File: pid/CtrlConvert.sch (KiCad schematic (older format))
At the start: 19 parts

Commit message: [pid] -
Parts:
- added C19, C20: 0.01u, ~, symbol C
- gave numbers to parts that had none: 18
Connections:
- wire segments 47 -> 51

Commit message: [pid] -
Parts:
- renumbered C18 to C17, C17 to C18, C20 to C19, C19 to C20, R37 to R40, R38 to R41, R41 to R42, R42 to R43, R39 to R44, R40 to R45, R44 to R46, R43 to R47, R46 to R48, R45 to R49, RV11 to RV10, RV10 to RV11, RV13 to RV12, RV12 to RV13
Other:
- moved on the sheet: C17, C18, C19, C20, R42, R43, R44, R45, R46, R47, R48, R49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

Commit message: [pid] net list
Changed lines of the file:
@@
 AR Path="/5355C3A0/53598F30/53556034" Ref="U17"  Part="1"
 AR Path="/5362BBC7/53598F30/53556034" Ref="U28"  Part="1"
-F 0 "U4" H 5200 2600 60  0000 C CNN
+F 0 "U28" H 5200 2600 60  0000 C CNN
 F 1 "MAX44251" H 5350 2250 60  0000 C CNN
 F 2 "~" H 4900 2400 60  0000 C CNN
@@
 AR Path="/5355C3A0/53598F30/53556043" Ref="U17"  Part="2"
 AR Path="/5362BBC7/53598F30/53556043" Ref="U28"  Part="2"
-F 0 "U4" H 5200 5450 60  0000 C CNN
+F 0 "U28" H 5200 5450 60  0000 C CNN
 F 1 "MAX44251" H 5350 5100 60  0000 C CNN
 F 2 "~" H 4900 5250 60  0000 C CNN
@@
 AR Path="/5355C3A0/53598F30/53556C67" Ref="R128"  Part="1"
 AR Path="/5362BBC7/53598F30/53556C67" Ref="R179"  Part="1"
-F 0 "R40" V 2680 2350 40  0000 C CNN
+F 0 "R179" V 2680 2350 40  0000 C CNN
 F 1 "100k" V 2607 2351 40  0000 C CNN
 F 2 "~" V 2530 2350 30  0000 C CNN
@@
 $EndComp
 $Comp
-L GND #PWR026
+L GND #PWR030
 U 1 1 53556C85
 P 2600 3300
-AR Path="/5355B409/53598F2F/53556C85" Ref="#PWR026"  Part="1"
-AR Path="/53562461/53555E75/53556C85" Ref="#PWR055"  Part="1"
-AR Path="/5355C3A0/53598F30/53556C85" Ref="#PWR082"  Part="1"
-AR Path="/5362BBC7/53598F30/53556C85" Ref="#PWR0120"  Part="1"
-F 0 "#PWR0120" H 2600 3300 30  0001 C CNN
+AR Path="/5355B409/53598F2F/53556C85" Ref="#PWR030"  Part="1"
+AR Path="/53562461/53555E75/53556C85" Ref="#PWR059"  Part="1"
+AR Path="/5355C3A0/53598F30/53556C85" Ref="#PWR086"  Part="1"
+AR Path="/5362BBC7/53598F30/53556C85" Ref="#PWR0124"  Part="1"
+F 0 "#PWR0124" H 2600 3300 30  0001 C CNN
 F 1 "GND" H 2600 3230 30  0001 C CNN
 F 2 "" H 2600 3300 60  0000 C CNN
@@
 AR Path="/5355C3A0/53598F30/53556CAF" Ref="R129"  Part="1"
 AR Path="/5362BBC7/53598F30/53556CAF" Ref="R180"  Part="1"
-F 0 "R41" V 2680 2950 40  0000 C CNN
+F 0 "R180" V 2680 2950 40  0000 C CNN
 F 1 "2k" V 2607 2951 40  0000 C CNN
 F 2 "~" V 2530 2950 30  0000 C CNN
@@
 AR Path="/5355C3A0/53598F30/53556D28" Ref="C67"  Part="1"
 AR Path="/5362BBC7/53598F30/53556D28" Ref="C102"  Part="1"
-F 0 "C16" H 2400 3050 40  0000 L CNN
+F 0 "C102" H 2400 3050 40  0000 L CNN
 F 1 "10u" H 2406 2865 40  0000 L CNN
 F 2 "~" H 2438 2800 30  0000 C CNN
@@
 AR Path="/5355C3A0/53598F30/53556F13" Ref="RV40"  Part="1"
 AR Path="/5362BBC7/53598F30/53556F13" Ref="RV54"  Part="1"
-F 0 "RV13" H 5050 4550 50  0000 C CNN
+F 0 "RV54" H 5050 4550 50  0000 C CNN
 F 1 "200k" H 5050 4650 50  0000 C CNN
 F 2 "~" H 5050 4650 60  0000 C CNN
@@
 AR Path="/5355C3A0/53598F30/53556F19" Ref="RV38"  Part="1"
 AR Path="/5362BBC7/53598F30/53556F19" Ref="RV52"  Part="1"
-F 0 "RV11" H 3850 4550 50  0000 C CNN
+F 0 "RV52" H 3850 4550 50  0000 C CNN
 F 1 "20k" H 3850 4650 50  0000 C CNN
 F 2 "~" H 3850 4650 60  0000 C CNN
@@
 AR Path="/5355C3A0/53598F30/53556FB4" Ref="R137"  Part="1"
 AR Path="/5362BBC7/53598F30/53556FB4" Ref="R188"  Part="1"
-F 0 "R49" V 5480 4950 40  0000 C CNN
+F 0 "R188" V 5480 4950 40  0000 C CNN
 F 1 "20k" V 5407 4951 40  0000 C CNN
 F 2 "~" V 5330 4950 30  0000 C CNN
@@
 AR Path="/5355C3A0/53598F30/5355702B" Ref="R135"  Part="1"
 AR Path="/5362BBC7/53598F30/5355702B" Ref="R186"  Part="1"
-F 0 "R47" V 4430 4650 40  0000 C CNN
+F 0 "R186" V 4430 4650 40  0000 C CNN
 F 1 "20k" V 4357 4651 40  0000 C CNN
 F 2 "~" V 4280 4650 30  0000 C CNN
@@
 AR Path="/5355C3A0/53598F30/53557349" Ref="R132"  Part="1"
 AR Path="/5362BBC7/53598F30/53557349" Ref="R183"  Part="1"
-F 0 "R44" V 3930 4050 40  0000 C CNN
+F 0 "R183" V 3930 4050 40  0000 C CNN
 F 1 "2k" V 3857 4051 40  0000 C CNN
 F 2 "~" V 3780 4050 30  0000 C CNN
@@
 AR Path="/5355C3A0/53598F30/5355734F" Ref="R133"  Part="1"
 AR Path="/5362BBC7/53598F30/5355734F" Ref="R184"  Part="1"
-F 0 "R45" V 3930 5250 40  0000 C CNN
+F 0 "R184" V 3930 5250 40  0000 C CNN
 F 1 "2k" V 3857 5251 40  0000 C CNN
 F 2 "~" V 3780 5250 30  0000 C CNN
@@
 AR Path="/5355C3A0/53598F30/53557785" Ref="RV37"  Part="1"
 AR Path="/5362BBC7/53598F30/53557785" Ref="RV51"  Part="1"
-F 0 "RV10" H 3850 2400 50  0000 C CNN
+F 0 "RV51" H 3850 2400 50  0000 C CNN
 F 1 "20k" H 3850 2500 50  0000 C CNN
 F 2 "~" H 3850 2500 60  0000 C CNN
@@
 AR Path="/5355C3A0/53598F30/5355778B" Ref="R130"  Part="1"
 AR Path="/5362BBC7/53598F30/5355778B" Ref="R181"  Part="1"
-F 0 "R42" V 3930 1900 40  0000 C CNN
+F 0 "R181" V 3930 1900 40  0000 C CNN
 F 1 "2k" V 3857 1901 40  0000 C CNN
 F 2 "~" V 3780 1900 30  0000 C CNN
@@
 AR Path="/5355C3A0/53598F30/53557791" Ref="R131"  Part="1"
 AR Path="/5362BBC7/53598F30/53557791" Ref="R182"  Part="1"
-F 0 "R43" V 3930 3100 40  0000 C CNN
+F 0 "R182" V 3930 3100 40  0000 C CNN
 F 1 "2k" V 3857 3101 40  0000 C CNN
 F 2 "~" V 3780 3100 30  0000 C CNN
@@
 AR Path="/5355C3A0/53598F30/5355779F" Ref="R134"  Part="1"
 AR Path="/5362BBC7/53598F30/5355779F" Ref="R185"  Part="1"
-F 0 "R46" V 4430 2300 40  0000 C CNN
+F 0 "R185" V 4430 2300 40  0000 C CNN
 F 1 "20k" V 4357 2301 40  0000 C CNN
 F 2 "~" V 4280 2300 30  0000 C CNN
@@
 AR Path="/5355C3A0/53598F30/535579B2" Ref="RV39"  Part="1"
 AR Path="/5362BBC7/53598F30/535579B2" Ref="RV53"  Part="1"
-F 0 "RV12" H 5050 1700 50  0000 C CNN
+F 0 "RV53" H 5050 1700 50  0000 C CNN
 F 1 "200k" H 5050 1800 50  0000 C CNN
 F 2 "~" H 5050 1800 60  0000 C CNN
@@
 AR Path="/5355C3A0/53598F30/535579B8" Ref="R136"  Part="1"
 AR Path="/5362BBC7/53598F30/535579B8" Ref="R187"  Part="1"
-F 0 "R48" V 5480 2100 40  0000 C CNN
+F 0 "R187" V 5480 2100 40  0000 C CNN
 F 1 "20k" V 5407 2101 40  0000 C CNN
 F 2 "~" V 5330 2100 30  0000 C CNN
@@
 AR Path="/5355C3A0/53598F30/53557D04" Ref="C69"  Part="1"
 AR Path="/5362BBC7/53598F30/53557D04" Ref="C104"  Part="1"
-F 0 "C18" H 4050 5000 40  0000 L CNN
+F 0 "C104" H 4050 5000 40  0000 L CNN
 F 1 "10u" H 4056 4815 40  0000 L CNN
 F 2 "~" H 4088 4750 30  0000 C CNN
@@
 AR Path="/5355C3A0/53598F30/53557D0A" Ref="C68"  Part="1"
 AR Path="/5362BBC7/53598F30/53557D0A" Ref="C103"  Part="1"
-F 0 "C17" H 4050 2850 40  0000 L CNN
+F 0 "C103" H 4050 2850 40  0000 L CNN
 F 1 "10u" H 4056 2665 40  0000 L CNN
 F 2 "~" H 4088 2600 30  0000 C CNN
@@
 $EndComp
 $Comp
-L GND #PWR027
+L GND #PWR031
 U 1 1 53557D10
 P 4050 5200
-AR Path="/5355B409/53598F2F/53557D10" Ref="#PWR027"  Part="1"
-AR Path="/53562461/53555E75/53557D10" Ref="#PWR056"  Part="1"
-AR Path="/5355C3A0/53598F30/53557D10" Ref="#PWR083"  Part="1"
-AR Path="/5362BBC7/53598F30/53557D10" Ref="#PWR0121"  Part="1"
-F 0 "#PWR0121" H 4050 5200 30  0001 C CNN
+AR Path="/5355B409/53598F2F/53557D10" Ref="#PWR031"  Part="1"
+AR Path="/53562461/53555E75/53557D10" Ref="#PWR060"  Part="1"
+AR Path="/5355C3A0/53598F30/53557D10" Ref="#PWR087"  Part="1"
+AR Path="/5362BBC7/53598F30/53557D10" Ref="#PWR0125"  Part="1"
+F 0 "#PWR0125" H 4050 5200 30  0001 C CNN
 F 1 "GND" H 4050 5130 30  0001 C CNN
 F 2 "" H 4050 5200 60  0000 C CNN
@@
 $EndComp
 $Comp
-L GND #PWR028
+L GND #PWR032
 U 1 1 53557D16
 P 4050 3050
-AR Path="/5355B409/53598F2F/53557D16" Ref="#PWR028"  Part="1"
-AR Path="/53562461/53555E75/53557D16" Ref="#PWR057"  Part="1"
-AR Path="/5355C3A0/53598F30/53557D16" Ref="#PWR084"  Part="1"
-AR Path="/5362BBC7/53598F30/53557D16" Ref="#PWR0122"  Part="1"
-F 0 "#PWR0122" H 4050 3050 30  0001 C CNN
+AR Path="/5355B409/53598F2F/53557D16" Ref="#PWR032"  Part="1"
+AR Path="/53562461/53555E75/53557D16" Ref="#PWR061"  Part="1"
+AR Path="/5355C3A0/53598F30/53557D16" Ref="#PWR088"  Part="1"
+AR Path="/5362BBC7/53598F30/53557D16" Ref="#PWR0126"  Part="1"
+F 0 "#PWR0126" H 4050 3050 30  0001 C CNN
 F 1 "GND" H 4050 2980 30  0001 C CNN
 F 2 "" H 4050 3050 60  0000 C CNN
@@
 AR Path="/5355C3A0/53598F30/535967B0" Ref="C71"  Part="1"
 AR Path="/5362BBC7/53598F30/535967B0" Ref="C106"  Part="1"
-F 0 "C20" H 4350 5200 40  0000 L CNN
+F 0 "C106" H 4350 5200 40  0000 L CNN
 F 1 "0.01u" H 4356 5015 40  0000 L CNN
 F 2 "~" H 4388 4950 30  0000 C CNN
@@
 AR Path="/5355C3A0/53598F30/535967B6" Ref="C70"  Part="1"
 AR Path="/5362BBC7/53598F30/535967B6" Ref="C105"  Part="1"
-F 0 "C19" H 4350 1900 40  0000 L CNN
+F 0 "C105" H 4350 1900 40  0000 L CNN
 F 1 "0.01u" H 4356 1715 40  0000 L CNN
 F 2 "~" H 4388 1650 30  0000 C CNN
@@
 $EndComp
 $Comp
-L GND #PWR029
+L GND #PWR033
 U 1 1 535967BC
 P 4350 5450
-AR Path="/5355B409/53598F2F/535967BC" Ref="#PWR029"  Part="1"
-AR Path="/53562461/53555E75/535967BC" Ref="#PWR058"  Part="1"
-AR Path="/5355C3A0/53598F30/535967BC" Ref="#PWR085"  Part="1"
-AR Path="/5362BBC7/53598F30/535967BC" Ref="#PWR0123"  Part="1"
-F 0 "#PWR0123" H 4350 5450 30  0001 C CNN
+AR Path="/5355B409/53598F2F/535967BC" Ref="#PWR033"  Part="1"
+AR Path="/53562461/53555E75/535967BC" Ref="#PWR062"  Part="1"
+AR Path="/5355C3A0/53598F30/535967BC" Ref="#PWR089"  Part="1"
+AR Path="/5362BBC7/53598F30/535967BC" Ref="#PWR0127"  Part="1"
+F 0 "#PWR0127" H 4350 5450 30  0001 C CNN
 F 1 "GND" H 4350 5380 30  0001 C CNN
 F 2 "" H 4350 5450 60  0000 C CNN
@@
 $EndComp
 $Comp
-L GND #PWR030
+L GND #PWR034
 U 1 1 535967C2
 P 4000 1950
-AR Path="/5355B409/53598F2F/535967C2" Ref="#PWR030"  Part="1"
-AR Path="/53562461/53555E75/535967C2" Ref="#PWR059"  Part="1"
-AR Path="/5355C3A0/53598F30/535967C2" Ref="#PWR086"  Part="1"
-AR Path="/5362BBC7/53598F30/535967C2" Ref="#PWR0124"  Part="1"
-F 0 "#PWR0124" H 4000 1950 30  0001 C CNN
+AR Path="/5355B409/53598F2F/535967C2" Ref="#PWR034"  Part="1"
+AR Path="/53562461/53555E75/535967C2" Ref="#PWR063"  Part="1"
+AR Path="/5355C3A0/53598F30/535967C2" Ref="#PWR090"  Part="1"
+AR Path="/5362BBC7/53598F30/535967C2" Ref="#PWR0128"  Part="1"
+F 0 "#PWR0128" H 4000 1950 30  0001 C CNN
 F 1 "GND" H 4000 1880 30  0001 C CNN
 F 2 "" H 4000 1950 60  0000 C CNN

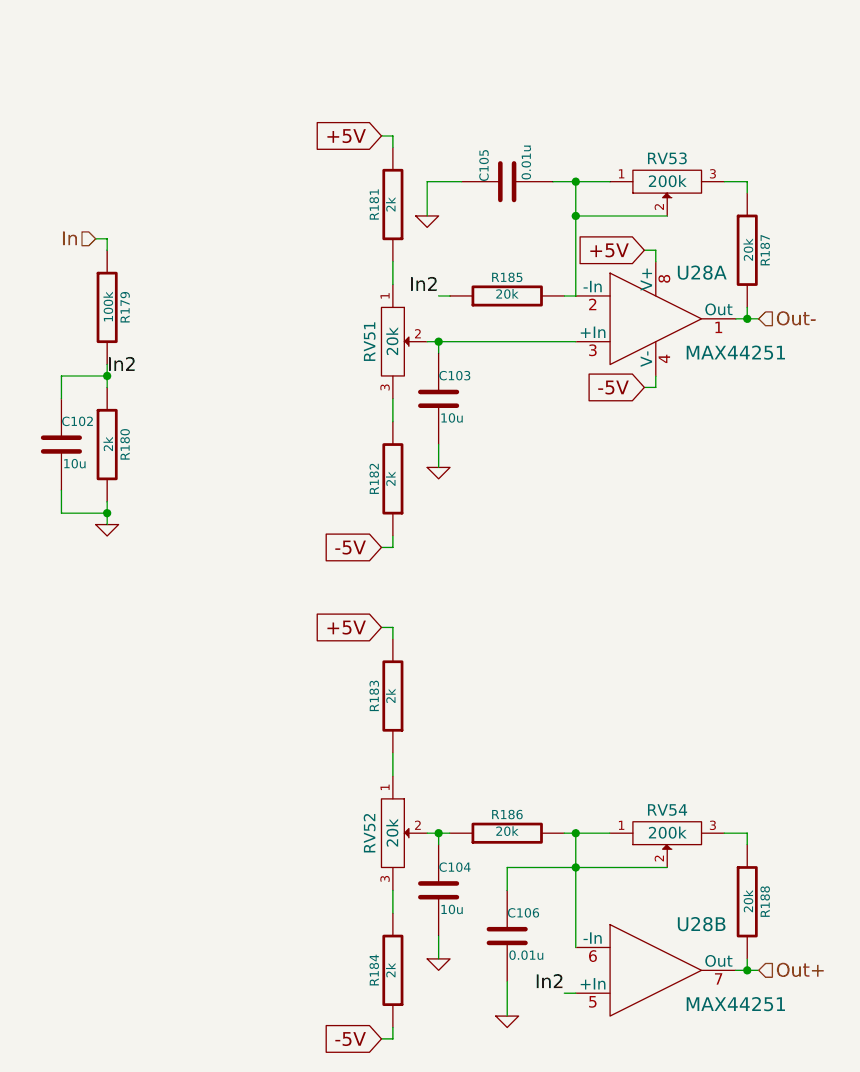
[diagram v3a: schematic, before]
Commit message: [pid] more capacitors, layout
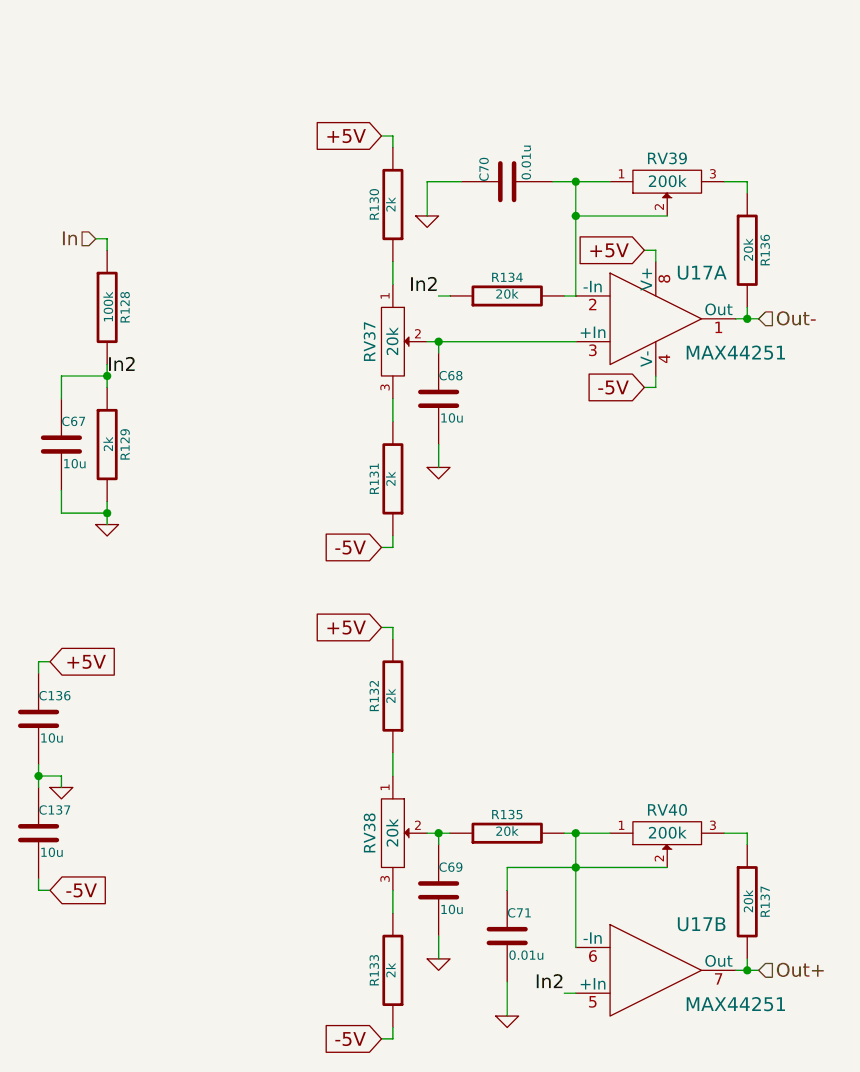
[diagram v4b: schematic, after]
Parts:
- added C132, C133: 10u, ~, symbol C
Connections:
- net +5V: now also C132.1
- net -5V: now also C133.2
- net GND: now also C132.2, C133.1

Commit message: [pid] update
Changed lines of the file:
@@
 Sheet 30 53
 Title ""
-Date "19 may 2014"
+Date "28 may 2014"
 Rev ""
 Comp ""
@@
 AR Path="/5355C3A0/53598F30/53556034" Ref="U17"  Part="1"
 AR Path="/5362BBC7/53598F30/53556034" Ref="U28"  Part="1"
-F 0 "U17" H 5200 2600 60  0000 C CNN
+F 0 "U28" H 5200 2600 60  0000 C CNN
 F 1 "MAX44251" H 5350 2250 60  0000 C CNN
 F 2 "~" H 4900 2400 60  0000 C CNN
@@
 AR Path="/5355C3A0/53598F30/53556043" Ref="U17"  Part="2"
 AR Path="/5362BBC7/53598F30/53556043" Ref="U28"  Part="2"
-F 0 "U17" H 5200 5450 60  0000 C CNN
+F 0 "U28" H 5200 5450 60  0000 C CNN
 F 1 "MAX44251" H 5350 5100 60  0000 C CNN
 F 2 "~" H 4900 5250 60  0000 C CNN
@@
 AR Path="/5355C3A0/53598F30/53556C67" Ref="R128"  Part="1"
 AR Path="/5362BBC7/53598F30/53556C67" Ref="R179"  Part="1"
-F 0 "R128" V 2680 2350 40  0000 C CNN
+F 0 "R179" V 2680 2350 40  0000 C CNN
 F 1 "100k" V 2607 2351 40  0000 C CNN
 F 2 "~" V 2530 2350 30  0000 C CNN
@@
 AR Path="/5355C3A0/53598F30/53556C85" Ref="#PWR088"  Part="1"
 AR Path="/5362BBC7/53598F30/53556C85" Ref="#PWR0127"  Part="1"
-F 0 "#PWR088" H 2600 3300 30  0001 C CNN
+F 0 "#PWR0127" H 2600 3300 30  0001 C CNN
 F 1 "GND" H 2600 3230 30  0001 C CNN
 F 2 "" H 2600 3300 60  0000 C CNN
@@
 AR Path="/5355C3A0/53598F30/53556CAF" Ref="R129"  Part="1"
 AR Path="/5362BBC7/53598F30/53556CAF" Ref="R180"  Part="1"
-F 0 "R129" V 2680 2950 40  0000 C CNN
+F 0 "R180" V 2680 2950 40  0000 C CNN
 F 1 "2k" V 2607 2951 40  0000 C CNN
 F 2 "~" V 2530 2950 30  0000 C CNN
@@
 AR Path="/5355C3A0/53598F30/53556D28" Ref="C67"  Part="1"
 AR Path="/5362BBC7/53598F30/53556D28" Ref="C102"  Part="1"
-F 0 "C67" H 2400 3050 40  0000 L CNN
+F 0 "C102" H 2400 3050 40  0000 L CNN
 F 1 "10u" H 2406 2865 40  0000 L CNN
 F 2 "~" H 2438 2800 30  0000 C CNN
@@
 AR Path="/5355C3A0/53598F30/53556F13" Ref="RV40"  Part="1"
 AR Path="/5362BBC7/53598F30/53556F13" Ref="RV54"  Part="1"
-F 0 "RV40" H 5050 4550 50  0000 C CNN
+F 0 "RV54" H 5050 4550 50  0000 C CNN
 F 1 "200k" H 5050 4650 50  0000 C CNN
 F 2 "~" H 5050 4650 60  0000 C CNN
@@
 AR Path="/5355C3A0/53598F30/53556F19" Ref="RV38"  Part="1"
 AR Path="/5362BBC7/53598F30/53556F19" Ref="RV52"  Part="1"
-F 0 "RV38" H 3850 4550 50  0000 C CNN
+F 0 "RV52" H 3850 4550 50  0000 C CNN
 F 1 "20k" H 3850 4650 50  0000 C CNN
 F 2 "~" H 3850 4650 60  0000 C CNN
@@
 AR Path="/5355C3A0/53598F30/53556FB4" Ref="R137"  Part="1"
 AR Path="/5362BBC7/53598F30/53556FB4" Ref="R188"  Part="1"
-F 0 "R137" V 5480 4950 40  0000 C CNN
+F 0 "R188" V 5480 4950 40  0000 C CNN
 F 1 "20k" V 5407 4951 40  0000 C CNN
 F 2 "~" V 5330 4950 30  0000 C CNN
@@
 AR Path="/5355C3A0/53598F30/5355702B" Ref="R135"  Part="1"
 AR Path="/5362BBC7/53598F30/5355702B" Ref="R186"  Part="1"
-F 0 "R135" V 4430 4650 40  0000 C CNN
+F 0 "R186" V 4430 4650 40  0000 C CNN
 F 1 "20k" V 4357 4651 40  0000 C CNN
 F 2 "~" V 4280 4650 30  0000 C CNN
@@
 AR Path="/5355C3A0/53598F30/53557349" Ref="R132"  Part="1"
 AR Path="/5362BBC7/53598F30/53557349" Ref="R183"  Part="1"
-F 0 "R132" V 3930 4050 40  0000 C CNN
+F 0 "R183" V 3930 4050 40  0000 C CNN
 F 1 "2k" V 3857 4051 40  0000 C CNN
 F 2 "~" V 3780 4050 30  0000 C CNN
@@
 AR Path="/5355C3A0/53598F30/5355734F" Ref="R133"  Part="1"
 AR Path="/5362BBC7/53598F30/5355734F" Ref="R184"  Part="1"
-F 0 "R133" V 3930 5250 40  0000 C CNN
+F 0 "R184" V 3930 5250 40  0000 C CNN
 F 1 "2k" V 3857 5251 40  0000 C CNN
 F 2 "~" V 3780 5250 30  0000 C CNN
@@
 AR Path="/5355C3A0/53598F30/53557785" Ref="RV37"  Part="1"
 AR Path="/5362BBC7/53598F30/53557785" Ref="RV51"  Part="1"
-F 0 "RV37" H 3850 2400 50  0000 C CNN
+F 0 "RV51" H 3850 2400 50  0000 C CNN
 F 1 "20k" H 3850 2500 50  0000 C CNN
 F 2 "~" H 3850 2500 60  0000 C CNN
@@
 AR Path="/5355C3A0/53598F30/5355778B" Ref="R130"  Part="1"
 AR Path="/5362BBC7/53598F30/5355778B" Ref="R181"  Part="1"
-F 0 "R130" V 3930 1900 40  0000 C CNN
+F 0 "R181" V 3930 1900 40  0000 C CNN
 F 1 "2k" V 3857 1901 40  0000 C CNN
 F 2 "~" V 3780 1900 30  0000 C CNN
@@
 AR Path="/5355C3A0/53598F30/53557791" Ref="R131"  Part="1"
 AR Path="/5362BBC7/53598F30/53557791" Ref="R182"  Part="1"
-F 0 "R131" V 3930 3100 40  0000 C CNN
+F 0 "R182" V 3930 3100 40  0000 C CNN
 F 1 "2k" V 3857 3101 40  0000 C CNN
 F 2 "~" V 3780 3100 30  0000 C CNN
@@
 AR Path="/5355C3A0/53598F30/5355779F" Ref="R134"  Part="1"
 AR Path="/5362BBC7/53598F30/5355779F" Ref="R185"  Part="1"
-F 0 "R134" V 4430 2300 40  0000 C CNN
+F 0 "R185" V 4430 2300 40  0000 C CNN
 F 1 "20k" V 4357 2301 40  0000 C CNN
 F 2 "~" V 4280 2300 30  0000 C CNN
@@
 AR Path="/5355C3A0/53598F30/535579B2" Ref="RV39"  Part="1"
 AR Path="/5362BBC7/53598F30/535579B2" Ref="RV53"  Part="1"
-F 0 "RV39" H 5050 1700 50  0000 C CNN
+F 0 "RV53" H 5050 1700 50  0000 C CNN
 F 1 "200k" H 5050 1800 50  0000 C CNN
 F 2 "~" H 5050 1800 60  0000 C CNN
@@
 AR Path="/5355C3A0/53598F30/535579B8" Ref="R136"  Part="1"
 AR Path="/5362BBC7/53598F30/535579B8" Ref="R187"  Part="1"
-F 0 "R136" V 5480 2100 40  0000 C CNN
+F 0 "R187" V 5480 2100 40  0000 C CNN
 F 1 "20k" V 5407 2101 40  0000 C CNN
 F 2 "~" V 5330 2100 30  0000 C CNN
@@
 AR Path="/5355C3A0/53598F30/53557D04" Ref="C69"  Part="1"
 AR Path="/5362BBC7/53598F30/53557D04" Ref="C104"  Part="1"
-F 0 "C69" H 4050 5000 40  0000 L CNN
+F 0 "C104" H 4050 5000 40  0000 L CNN
 F 1 "10u" H 4056 4815 40  0000 L CNN
 F 2 "~" H 4088 4750 30  0000 C CNN
@@
 AR Path="/5355C3A0/53598F30/53557D0A" Ref="C68"  Part="1"
 AR Path="/5362BBC7/53598F30/53557D0A" Ref="C103"  Part="1"
-F 0 "C68" H 4050 2850 40  0000 L CNN
+F 0 "C103" H 4050 2850 40  0000 L CNN
 F 1 "10u" H 4056 2665 40  0000 L CNN
 F 2 "~" H 4088 2600 30  0000 C CNN
@@
 AR Path="/5355C3A0/53598F30/53557D10" Ref="#PWR089"  Part="1"
 AR Path="/5362BBC7/53598F30/53557D10" Ref="#PWR0128"  Part="1"
-F 0 "#PWR089" H 4050 5200 30  0001 C CNN
+F 0 "#PWR0128" H 4050 5200 30  0001 C CNN
 F 1 "GND" H 4050 5130 30  0001 C CNN
 F 2 "" H 4050 5200 60  0000 C CNN
@@
 AR Path="/5355C3A0/53598F30/53557D16" Ref="#PWR090"  Part="1"
 AR Path="/5362BBC7/53598F30/53557D16" Ref="#PWR0129"  Part="1"
-F 0 "#PWR090" H 4050 3050 30  0001 C CNN
+F 0 "#PWR0129" H 4050 3050 30  0001 C CNN
 F 1 "GND" H 4050 2980 30  0001 C CNN
 F 2 "" H 4050 3050 60  0000 C CNN
@@
 AR Path="/5355C3A0/53598F30/535967B0" Ref="C71"  Part="1"
 AR Path="/5362BBC7/53598F30/535967B0" Ref="C106"  Part="1"
-F 0 "C71" H 4350 5200 40  0000 L CNN
+F 0 "C106" H 4350 5200 40  0000 L CNN
 F 1 "0.01u" H 4356 5015 40  0000 L CNN
 F 2 "~" H 4388 4950 30  0000 C CNN
@@
 AR Path="/5355C3A0/53598F30/535967B6" Ref="C70"  Part="1"
 AR Path="/5362BBC7/53598F30/535967B6" Ref="C105"  Part="1"
-F 0 "C70" H 4350 1900 40  0000 L CNN
+F 0 "C105" H 4350 1900 40  0000 L CNN
 F 1 "0.01u" H 4356 1715 40  0000 L CNN
 F 2 "~" H 4388 1650 30  0000 C CNN
@@
 AR Path="/5355C3A0/53598F30/535967BC" Ref="#PWR091"  Part="1"
 AR Path="/5362BBC7/53598F30/535967BC" Ref="#PWR0130"  Part="1"
-F 0 "#PWR091" H 4350 5450 30  0001 C CNN
+F 0 "#PWR0130" H 4350 5450 30  0001 C CNN
 F 1 "GND" H 4350 5380 30  0001 C CNN
 F 2 "" H 4350 5450 60  0000 C CNN
@@
 AR Path="/5355C3A0/53598F30/535967C2" Ref="#PWR092"  Part="1"
 AR Path="/5362BBC7/53598F30/535967C2" Ref="#PWR0131"  Part="1"
-F 0 "#PWR092" H 4000 1950 30  0001 C CNN
+F 0 "#PWR0131" H 4000 1950 30  0001 C CNN
 F 1 "GND" H 4000 1880 30  0001 C CNN
 F 2 "" H 4000 1950 60  0000 C CNN
@@
 AR Path="/5355C3A0/53598F30/5364299E" Ref="C136"  Part="1"
 AR Path="/5362BBC7/53598F30/5364299E" Ref="C138"  Part="1"
-F 0 "C136" H 2300 4250 40  0000 L CNN
+F 0 "C138" H 2300 4250 40  0000 L CNN
 F 1 "10u" H 2306 4065 40  0000 L CNN
 F 2 "~" H 2338 4000 30  0000 C CNN
@@
 AR Path="/5355C3A0/53598F30/536429A4" Ref="C137"  Part="1"
 AR Path="/5362BBC7/53598F30/536429A4" Ref="C139"  Part="1"
-F 0 "C137" H 2300 4750 40  0000 L CNN
+F 0 "C139" H 2300 4750 40  0000 L CNN
 F 1 "10u" H 2306 4565 40  0000 L CNN
 F 2 "~" H 2338 4500 30  0000 C CNN
@@
 AR Path="/5355C3A0/53598F30/536429AA" Ref="#PWR093"  Part="1"
 AR Path="/5362BBC7/53598F30/536429AA" Ref="#PWR0132"  Part="1"
-F 0 "#PWR093" H 2400 4450 30  0001 C CNN
+F 0 "#PWR0132" H 2400 4450 30  0001 C CNN
 F 1 "GND" H 2400 4380 30  0001 C CNN
 F 2 "" H 2400 4450 60  0000 C CNN
